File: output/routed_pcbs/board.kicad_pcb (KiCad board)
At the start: 2 copper layers, 122.3 x 101.1 mm, 48 parts, among them J1 Jumper, J2 Jumper

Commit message: finish up
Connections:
- MCU1 pad 25: B- -> Bminus
- MCU2 pad 25: B- -> Bminus
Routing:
- net Bplus: track 12.9 -> 66.2 mm
- net Bminus: track 3.03 -> 44.0 mm
- net B-: track 18.3 -> 0.00 mm
- net P6: track 164.4 -> 150.9 mm, vias 1 -> 0
- net B+: track 13.3 -> 0.00 mm
- net P1: track 18.3 -> 28.2 mm
- net P0: track 68.4 -> 70.3 mm
- net Braw: track 33.8 -> 32.7 mm
- net GND: track 97.8 -> 96.8 mm
- net P5: track 138.4 -> 139.0 mm

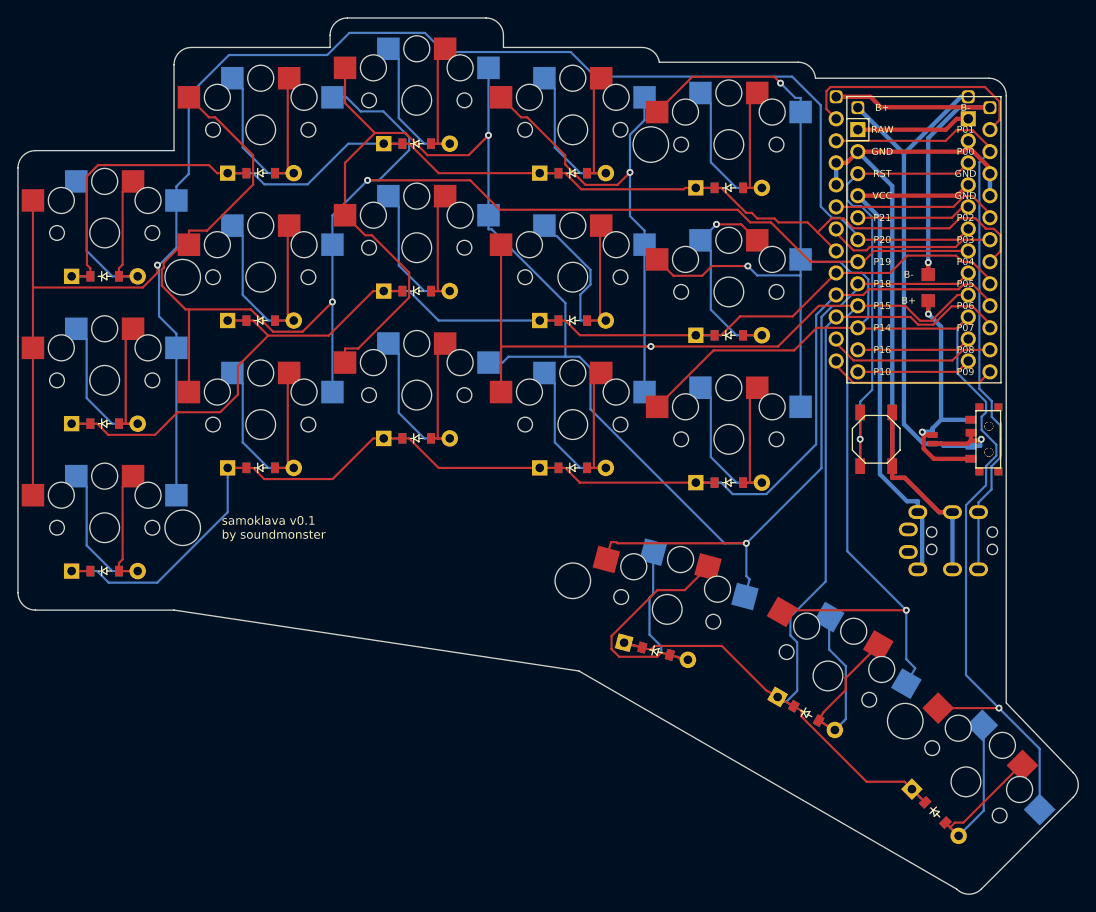
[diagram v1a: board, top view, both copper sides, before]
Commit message: Use a better reset button footprint (#6)
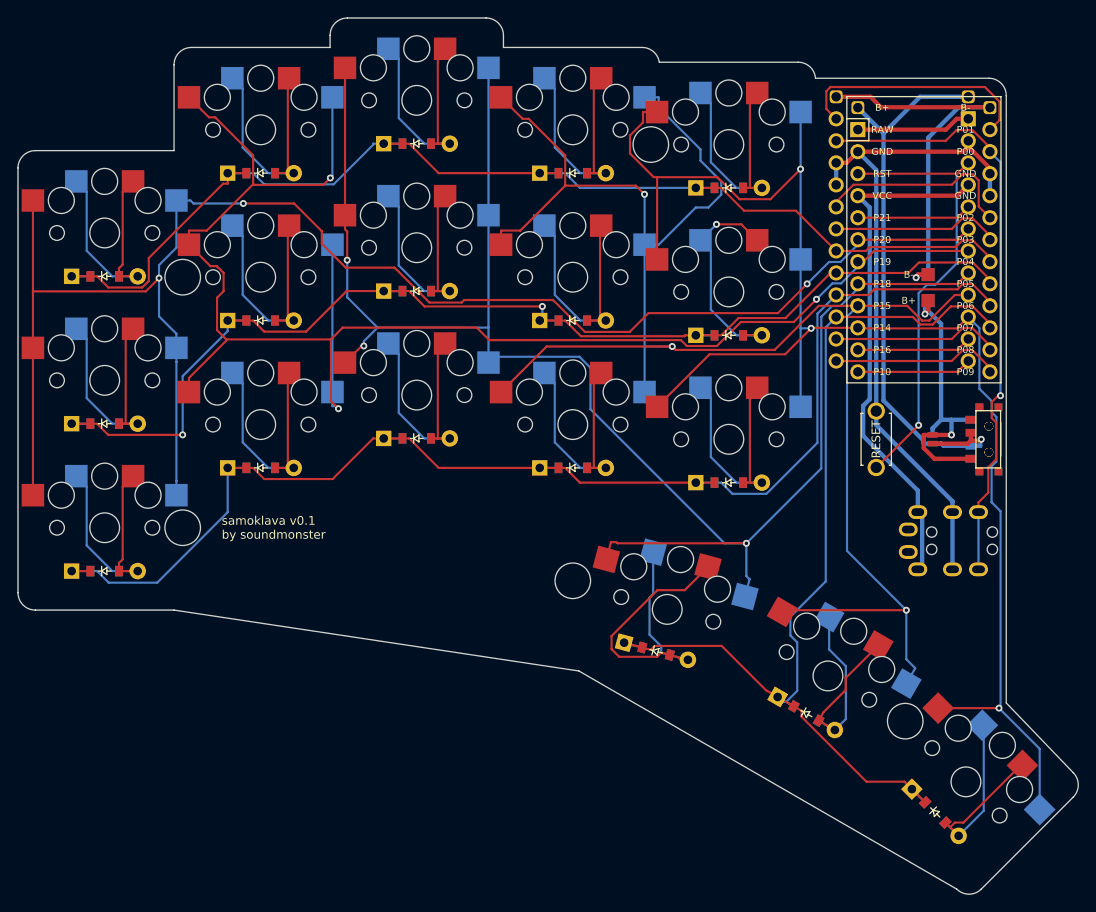
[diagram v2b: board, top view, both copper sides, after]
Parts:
- removed B2: , E73:SW_TACT_ALPS_SKQGABE010
- B1: footprint E73:SW_TACT_ALPS_SKQGABE010 -> kbd:ResetSW
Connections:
- B1 pad 1: GND -> RST
- B1 pad 2: RST -> GND
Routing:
- net P20: track 209.0 -> 188.8 mm, vias 1 -> 3
- net GND: track 96.8 -> 78.6 mm
- net P15: track 193.2 -> 209.8 mm
- net P14: track 199.7 -> 183.1 mm
- net P18: track 211.6 -> 198.7 mm, vias 2 -> 3
- net P4: track 146.8 -> 134.5 mm
- net P2: track 19.6 -> 23.5 mm
- net RST: track 56.0 -> 53.4 mm
- net Braw: track 32.7 -> 35.2 mm
- net P19: track 182.8 -> 184.7 mm, vias 2 -> 3
- net Bminus: track 44.0 -> 45.9 mm
- net Bplus: track 66.2 -> 67.6 mm
- net index_home: track 30.1 -> 29.0 mm
- net P5: track 139.0 -> 138.1 mm, vias 0 -> 2
- net P0: track 70.3 -> 69.9 mm, vias 0 -> 1
